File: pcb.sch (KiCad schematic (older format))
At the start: 36 parts, among them J1 230VAC IN, J10 DHT22 2, J11 DHT22 3, J12 LIGHTS, J2 12VDC IN, J3 40HAT, J4 CONN_01X02, J5 CONN_02X02, J6 FAN 1, J7 FAN 2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

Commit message: Rearranged connectors. Added early triac circuit.
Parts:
- added C1: 10u, Capacitor_SMD:CP_Elec_4x5.3, symbol Device:CP
- added Q6: BT136-600, Package_TO_SOT_THT:TO-220-3_Vertical, symbol Triac_Thyristor:BT136-600
- added R4, R5: 400R, Resistor_SMD:R_1206_3216Metric_Pad1.30x1.75mm_HandSolder, symbol Device:R
- added U1: MOC3043M, symbol Relay_SolidState:MOC3043M
- gave numbers to parts that had none: 8
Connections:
- wire segments 136 -> 152
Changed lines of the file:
@@
 	3200 3250 4400 3250
 $Comp
-L Connector_Generic:Conn_01x02 J?
+L Connector_Generic:Conn_01x02 J13
 U 1 1 5FD232CF
 P 12300 4350
-F 0 "J?" H 12380 4342 50  0000 L CNN
+F 0 "J13" H 12380 4342 50  0000 L CNN
 F 1 "Conn_01x02" H 12380 4251 50  0000 L CNN
 F 2 "Connector_PinHeader_2.54mm:PinHeader_1x02_P2.54mm_Vertical" H 12300 4350 50  0001 C CNN
@@
 $EndComp
 $Comp
-L power:GND #PWR?
+L power:GND #PWR0101
 U 1 1 5FD55316
 P 10750 6500
-F 0 "#PWR?" H 10750 6250 50  0001 C CNN
+F 0 "#PWR0101" H 10750 6250 50  0001 C CNN
 F 1 "GND" H 10750 6350 50  0000 C CNN
 F 2 "" H 10750 6500 50  0000 C CNN
@@
 FAN_1_OUT
 $Comp
-L Device:R R?
+L Device:R R1
 U 1 1 5FCE279C
 P 10250 6250
-F 0 "R?" V 10043 6250 50  0000 C CNN
+F 0 "R1" V 10043 6250 50  0000 C CNN
 F 1 "100R" V 10134 6250 50  0000 C CNN
 F 2 "Resistor_SMD:R_1206_3216Metric_Pad1.30x1.75mm_HandSolder" V 10180 6250 50  0001 C CNN
@@
 	11600 4450 12100 4450
 $Comp
-L Connector_Generic:Conn_01x02 J?
+L Connector_Generic:Conn_01x02 J14
 U 1 1 5FF3F3E5
 P 13700 4350
-F 0 "J?" H 13780 4342 50  0000 L CNN
+F 0 "J14" H 13780 4342 50  0000 L CNN
 F 1 "Conn_01x02" H 13780 4251 50  0000 L CNN
 F 2 "Connector_PinHeader_2.54mm:PinHeader_1x02_P2.54mm_Vertical" H 13700 4350 50  0001 C CNN
@@
 	13000 4450 13500 4450
 $Comp
-L Connector_Generic:Conn_01x02 J?
+L Connector_Generic:Conn_01x02 J15
 U 1 1 5FF44AFB
 P 15050 4350
-F 0 "J?" H 15130 4342 50  0000 L CNN
+F 0 "J15" H 15130 4342 50  0000 L CNN
 F 1 "Conn_01x02" H 15130 4251 50  0000 L CNN
 F 2 "Connector_PinHeader_2.54mm:PinHeader_1x02_P2.54mm_Vertical" H 15050 4350 50  0001 C CNN
@@
 	14350 4450 14850 4450
 $Comp
-L plantification:IRLIZ44N Q?
+L plantification:IRLIZ44N Q4
 U 1 1 5FF58F9B
 P 10650 7100
-F 0 "Q?" H 10855 7146 50  0000 L CNN
+F 0 "Q4" H 10855 7146 50  0000 L CNN
 F 1 "IRLU024NPBF" H 10855 7055 50  0000 L CNN
 F 2 "Package_TO_SOT_THT:TO-251-3-1EP_Horizontal_TabDown" H 10900 7025 50  0001 L CIN
@@
 $EndComp
 $Comp
-L power:GND #PWR?
+L power:GND #PWR0102
 U 1 1 5FF58FA1
 P 10750 7350
-F 0 "#PWR?" H 10750 7100 50  0001 C CNN
+F 0 "#PWR0102" H 10750 7100 50  0001 C CNN
 F 1 "GND" H 10750 7200 50  0000 C CNN
 F 2 "" H 10750 7350 50  0000 C CNN
@@
 FAN_2_OUT
 $Comp
-L Device:R R?
+L Device:R R2
 U 1 1 5FF58FAD
 P 10250 7100
-F 0 "R?" V 10043 7100 50  0000 C CNN
+F 0 "R2" V 10043 7100 50  0000 C CNN
 F 1 "100R" V 10134 7100 50  0000 C CNN
 F 2 "Resistor_SMD:R_1206_3216Metric_Pad1.30x1.75mm_HandSolder" V 10180 7100 50  0001 C CNN
@@
 	10100 7100 9500 7100
 $Comp
-L plantification:IRLIZ44N Q?
+L plantification:IRLIZ44N Q5
 U 1 1 5FF5F52E
 P 10650 7950
-F 0 "Q?" H 10855 7996 50  0000 L CNN
+F 0 "Q5" H 10855 7996 50  0000 L CNN
 F 1 "IRLU024NPBF" H 10855 7905 50  0000 L CNN
 F 2 "Package_TO_SOT_THT:TO-251-3-1EP_Horizontal_TabDown" H 10900 7875 50  0001 L CIN
@@
 $EndComp
 $Comp
-L power:GND #PWR?
+L power:GND #PWR0103
 U 1 1 5FF5F534
 P 10750 8200
-F 0 "#PWR?" H 10750 7950 50  0001 C CNN
+F 0 "#PWR0103" H 10750 7950 50  0001 C CNN
 F 1 "GND" H 10750 8050 50  0000 C CNN
 F 2 "" H 10750 8200 50  0000 C CNN
@@
 FAN_3_OUT
 $Comp
-L Device:R R?
+L Device:R R3
 U 1 1 5FF5F540
 P 10250 7950
-F 0 "R?" V 10043 7950 50  0000 C CNN
+F 0 "R3" V 10043 7950 50  0000 C CNN
 F 1 "100R" V 10134 7950 50  0000 C CNN
 F 2 "Resistor_SMD:R_1206_3216Metric_Pad1.30x1.75mm_HandSolder" V 10180 7950 50  0001 C CNN
@@
 Wire Wire Line
 	10100 7950 9500 7950
+$Comp
+L Relay_SolidState:MOC3043M U1
+U 1 1 5FCCF357
+P 13100 6550
+F 0 "U1" H 13100 6875 50  0000 C CNN
+F 1 "MOC3043M" H 13100 6784 50  0000 C CNN
+F 2 "" H 12900 6350 50  0001 L CIN
+F 3 "https://www.onsemi.com/pub/Collateral/MOC3043M-D.pdf" H 13100 6550 50  0001 L CNN
+	1    13100 6550
+	1    0    0    -1
+$EndComp
+$Comp
+L Device:R R4
+U 1 1 5FCD0D80
+P 12600 6450
+F 0 "R4" V 12393 6450 50  0000 C CNN
+F 1 "400R" V 12484 6450 50  0000 C CNN
+F 2 "Resistor_SMD:R_1206_3216Metric_Pad1.30x1.75mm_HandSolder" V 12530 6450 50  0001 C CNN
+F 3 "~" H 12600 6450 50  0001 C CNN
+	1    12600 6450
+	0    1    1    0
+$EndComp
+$Comp
+L Device:CP C1
+U 1 1 5FCD2BE2
+P 12300 6600
+F 0 "C1" H 12418 6646 50  0000 L CNN
+F 1 "10u" H 12418 6555 50  0000 L CNN
+F 2 "Capacitor_SMD:CP_Elec_4x5.3" H 12338 6450 50  0001 C CNN
+F 3 "~" H 12300 6600 50  0001 C CNN
+	1    12300 6600
+	1    0    0    -1
+$EndComp
+$Comp
+L Triac_Thyristor:BT136-600 Q6
+U 1 1 5FCD5F94
+P 14000 6600
+F 0 "Q6" H 14128 6646 50  0000 L CNN
+F 1 "BT136-600" H 14128 6555 50  0000 L CNN
+F 2 "Package_TO_SOT_THT:TO-220-3_Vertical" H 14200 6525 50  0001 L CIN
+F 3 "http://www.micropik.com/PDF/BT136-600.pdf" H 14000 6600 50  0001 L CNN
+	1    14000 6600
+	1    0    0    -1
+$EndComp
+$Comp
+L Device:R R5
+U 1 1 5FCD7A14
+P 13650 6450
+F 0 "R5" V 13443 6450 50  0000 C CNN
+F 1 "400R" V 13534 6450 50  0000 C CNN
+F 2 "Resistor_SMD:R_1206_3216Metric_Pad1.30x1.75mm_HandSolder" V 13580 6450 50  0001 C CNN
+F 3 "~" H 13650 6450 50  0001 C CNN
+	1    13650 6450
+	0    1    1    0
+$EndComp
+Wire Wire Line
+	12750 6450 12800 6450
+Wire Wire Line
+	12450 6450 12300 6450
+Connection ~ 12300 6450
+Wire Wire Line
+	12300 6450 11800 6450
+Wire Wire Line
+	12800 6650 12800 6750
+Wire Wire Line
+	12800 6750 12300 6750
+Wire Wire Line
+	11800 6750 12300 6750
+Connection ~ 12300 6750
+Wire Wire Line
+	13500 6450 13400 6450
+Wire Wire Line
+	13800 6450 14000 6450
+Wire Wire Line
+	13850 6700 13750 6700
+Wire Wire Line
+	13750 6700 13750 6650
+Wire Wire Line
+	13750 6650 13400 6650
+Wire Wire Line
+	14000 6750 14000 6900
+Wire Wire Line
+	14000 6450 14000 6300
+Connection ~ 14000 6450
+Wire Wire Line
+	14000 6300 14500 6300
+Wire Wire Line
+	14000 6900 14500 6900
+Text Label 14500 6900 2    50   ~ 0
+LIGHTS_L
+Text Label 14500 6300 2    50   ~ 0
+230VAC_L
+Text Label 13650 5900 2    50   ~ 0
+LIGHTS_N
+Text Label 12700 5900 0    50   ~ 0
+230VAC_N
+Wire Wire Line
+	12700 5900 13650 5900
 $EndSCHEMATC

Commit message: Set optoisolator and triac footprints
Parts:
- Q6: footprint Package_TO_SOT_THT:TO-220-3_Vertical -> Package_TO_SOT_THT:TO-220-3_Horizontal_TabDown
- U1: footprint (none) -> Package_DIP:DIP-6_W7.62mm
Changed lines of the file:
@@
 F 0 "U1" H 13100 6875 50  0000 C CNN
 F 1 "MOC3043M" H 13100 6784 50  0000 C CNN
-F 2 "" H 12900 6350 50  0001 L CIN
+F 2 "Package_DIP:DIP-6_W7.62mm" H 12900 6350 50  0001 L CIN
 F 3 "https://www.onsemi.com/pub/Collateral/MOC3043M-D.pdf" H 13100 6550 50  0001 L CNN
 	1    13100 6550
@@
 F 0 "Q6" H 14128 6646 50  0000 L CNN
 F 1 "BT136-600" H 14128 6555 50  0000 L CNN
-F 2 "Package_TO_SOT_THT:TO-220-3_Vertical" H 14200 6525 50  0001 L CIN
+F 2 "Package_TO_SOT_THT:TO-220-3_Horizontal_TabDown" H 14200 6525 50  0001 L CIN
 F 3 "http://www.micropik.com/PDF/BT136-600.pdf" H 14000 6600 50  0001 L CNN
 	1    14000 6600

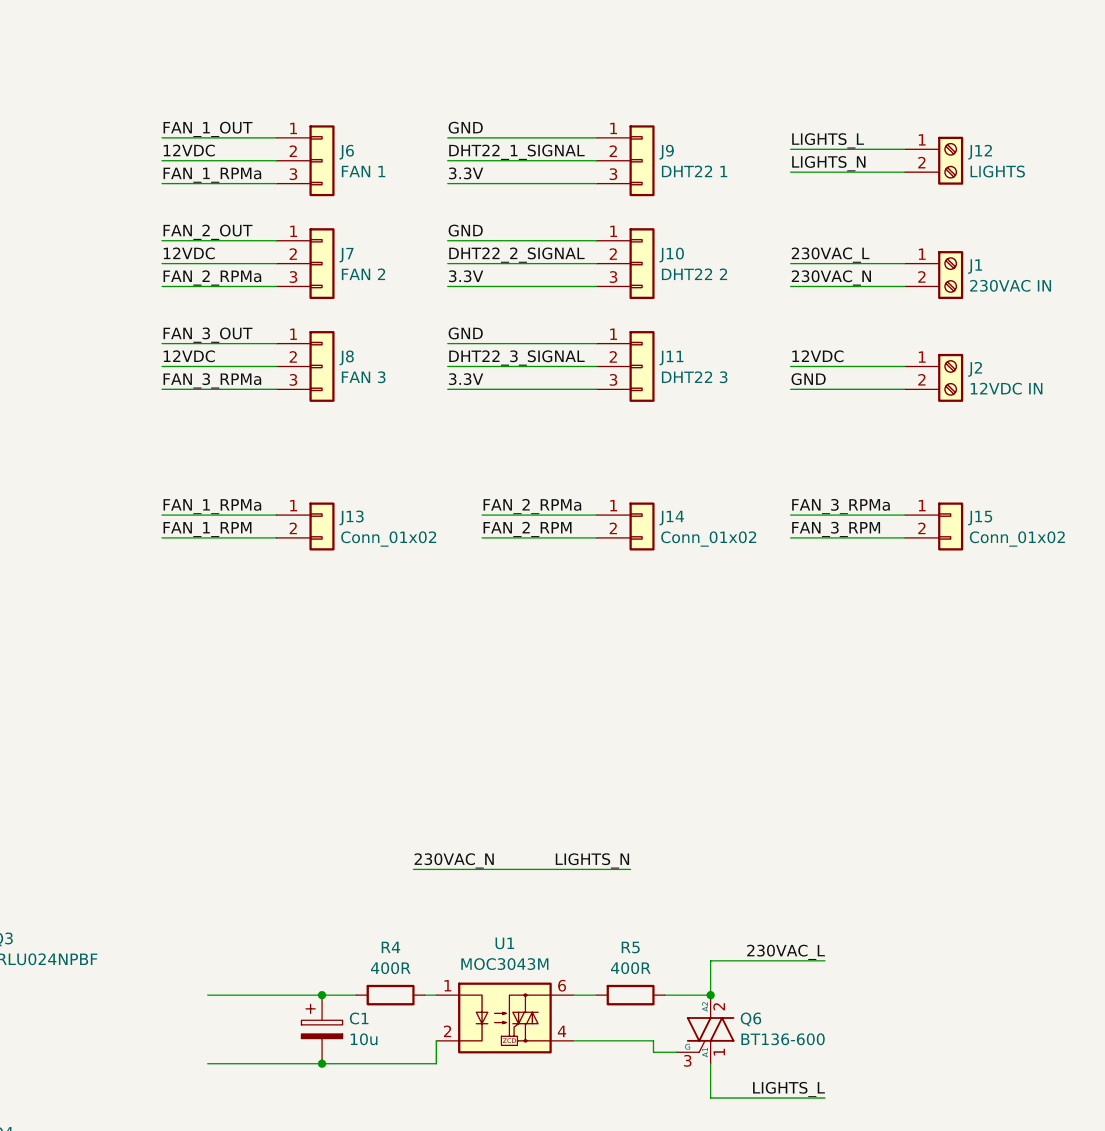
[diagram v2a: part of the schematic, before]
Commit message: Remove fan speed connectors
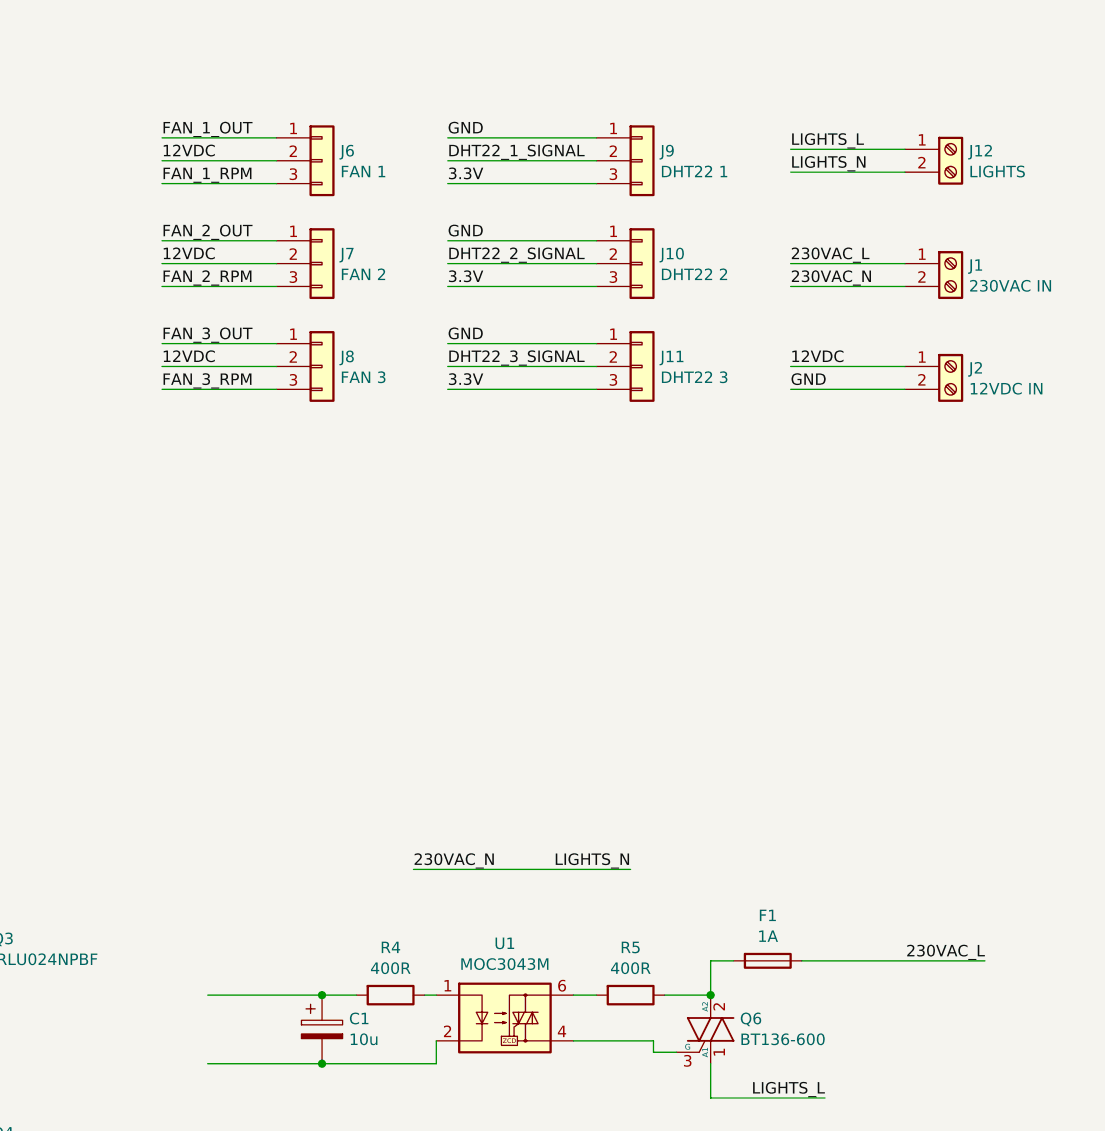
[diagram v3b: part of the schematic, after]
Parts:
- removed J13, J14, J15: Conn_01x02, Connector_PinHeader_2.54mm:PinHeader_1x02_P2.54mm_Vertical, symbol Connector_Generic:Conn_01x02
- added F1: 1A, Fuse:Fuseholder_Cylinder-5x20mm_Schurter_0031_8201_Horizontal_Open, symbol Device:Fuse
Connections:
- net labels removed: FAN_1_RPMa, FAN_2_RPMa, FAN_3_RPMa
- wire segments 152 -> 147
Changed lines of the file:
@@
 12VDC
 Text Label 11600 2900 0    50   ~ 0
-FAN_1_RPMa
+FAN_1_RPM
 Text Label 14350 3250 0    50   ~ 0
 230VAC_L
@@
 FAN_3_OUT
 Text Label 11600 3350 0    50   ~ 0
-FAN_2_RPMa
+FAN_2_RPM
 Text Label 11600 3800 0    50   ~ 0
-FAN_3_RPMa
+FAN_3_RPM
 Text Label 12850 2900 0    50   ~ 0
 3.3V
@@
 	3200 3250 4400 3250
 $Comp
-L Connector_Generic:Conn_01x02 J13
-U 1 1 5FD232CF
-P 12300 4350
-F 0 "J13" H 12380 4342 50  0000 L CNN
-F 1 "Conn_01x02" H 12380 4251 50  0000 L CNN
-F 2 "Connector_PinHeader_2.54mm:PinHeader_1x02_P2.54mm_Vertical" H 12300 4350 50  0001 C CNN
-F 3 "~" H 12300 4350 50  0001 C CNN
-	1    12300 4350
-	1    0    0    -1
-$EndComp
-$Comp
 L power:GND #PWR0101
 U 1 1 5FD55316
@@
 Wire Wire Line
 	14350 3350 14850 3350
-Text Label 11600 4350 0    50   ~ 0
-FAN_1_RPMa
-Text Label 11600 4450 0    50   ~ 0
-FAN_1_RPM
-Wire Wire Line
-	11600 4350 12100 4350
-Wire Wire Line
-	11600 4450 12100 4450
-$Comp
-L Connector_Generic:Conn_01x02 J14
-U 1 1 5FF3F3E5
-P 13700 4350
-F 0 "J14" H 13780 4342 50  0000 L CNN
-F 1 "Conn_01x02" H 13780 4251 50  0000 L CNN
-F 2 "Connector_PinHeader_2.54mm:PinHeader_1x02_P2.54mm_Vertical" H 13700 4350 50  0001 C CNN
-F 3 "~" H 13700 4350 50  0001 C CNN
-	1    13700 4350
-	1    0    0    -1
-$EndComp
-Text Label 13000 4350 0    50   ~ 0
-FAN_2_RPMa
-Text Label 13000 4450 0    50   ~ 0
-FAN_2_RPM
-Wire Wire Line
-	13000 4350 13500 4350
-Wire Wire Line
-	13000 4450 13500 4450
-$Comp
-L Connector_Generic:Conn_01x02 J15
-U 1 1 5FF44AFB
-P 15050 4350
-F 0 "J15" H 15130 4342 50  0000 L CNN
-F 1 "Conn_01x02" H 15130 4251 50  0000 L CNN
-F 2 "Connector_PinHeader_2.54mm:PinHeader_1x02_P2.54mm_Vertical" H 15050 4350 50  0001 C CNN
-F 3 "~" H 15050 4350 50  0001 C CNN
-	1    15050 4350
-	1    0    0    -1
-$EndComp
-Text Label 14350 4350 0    50   ~ 0
-FAN_3_RPMa
-Text Label 14350 4450 0    50   ~ 0
-FAN_3_RPM
-Wire Wire Line
-	14350 4350 14850 4350
-Wire Wire Line
-	14350 4450 14850 4450
 $Comp
 L plantification:IRLIZ44N Q4
@@
 Connection ~ 14000 6450
 Wire Wire Line
-	14000 6300 14500 6300
-Wire Wire Line
 	14000 6900 14500 6900
 Text Label 14500 6900 2    50   ~ 0
 LIGHTS_L
-Text Label 14500 6300 2    50   ~ 0
+Text Label 15200 6300 2    50   ~ 0
 230VAC_L
 Text Label 13650 5900 2    50   ~ 0
@@
 Wire Wire Line
 	12700 5900 13650 5900
+$Comp
+L Device:Fuse F1
+U 1 1 5FCC3312
+P 14250 6300
+F 0 "F1" V 14053 6300 50  0000 C CNN
+F 1 "1A" V 14144 6300 50  0000 C CNN
+F 2 "Fuse:Fuseholder_Cylinder-5x20mm_Schurter_0031_8201_Horizontal_Open" V 14180 6300 50  0001 C CNN
+F 3 "~" H 14250 6300 50  0001 C CNN
+	1    14250 6300
+	0    1    1    0
+$EndComp
+Wire Wire Line
+	14000 6300 14100 6300
+Wire Wire Line
+	14400 6300 15200 6300
 $EndSCHEMATC

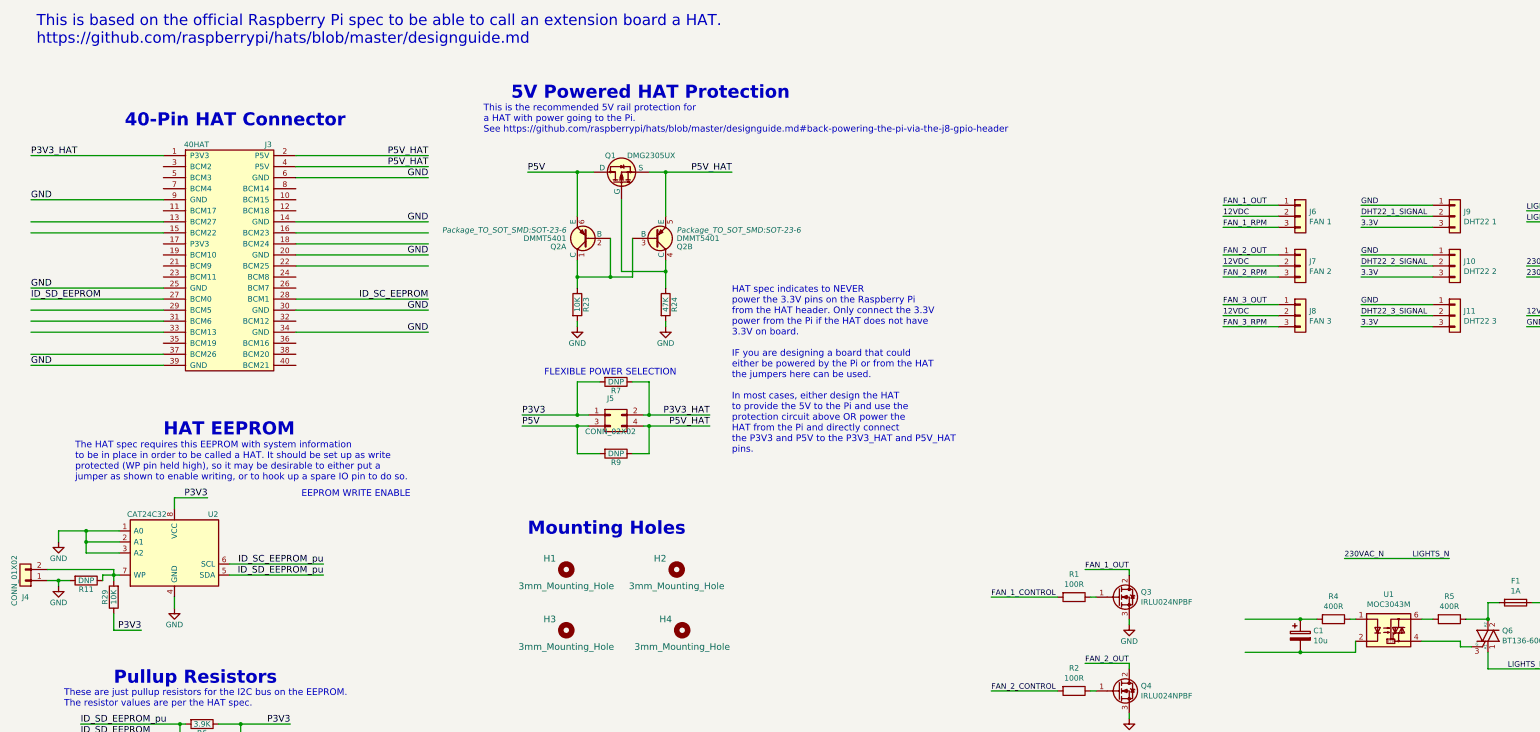
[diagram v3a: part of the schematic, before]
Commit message: Connect devices to the RPi connector
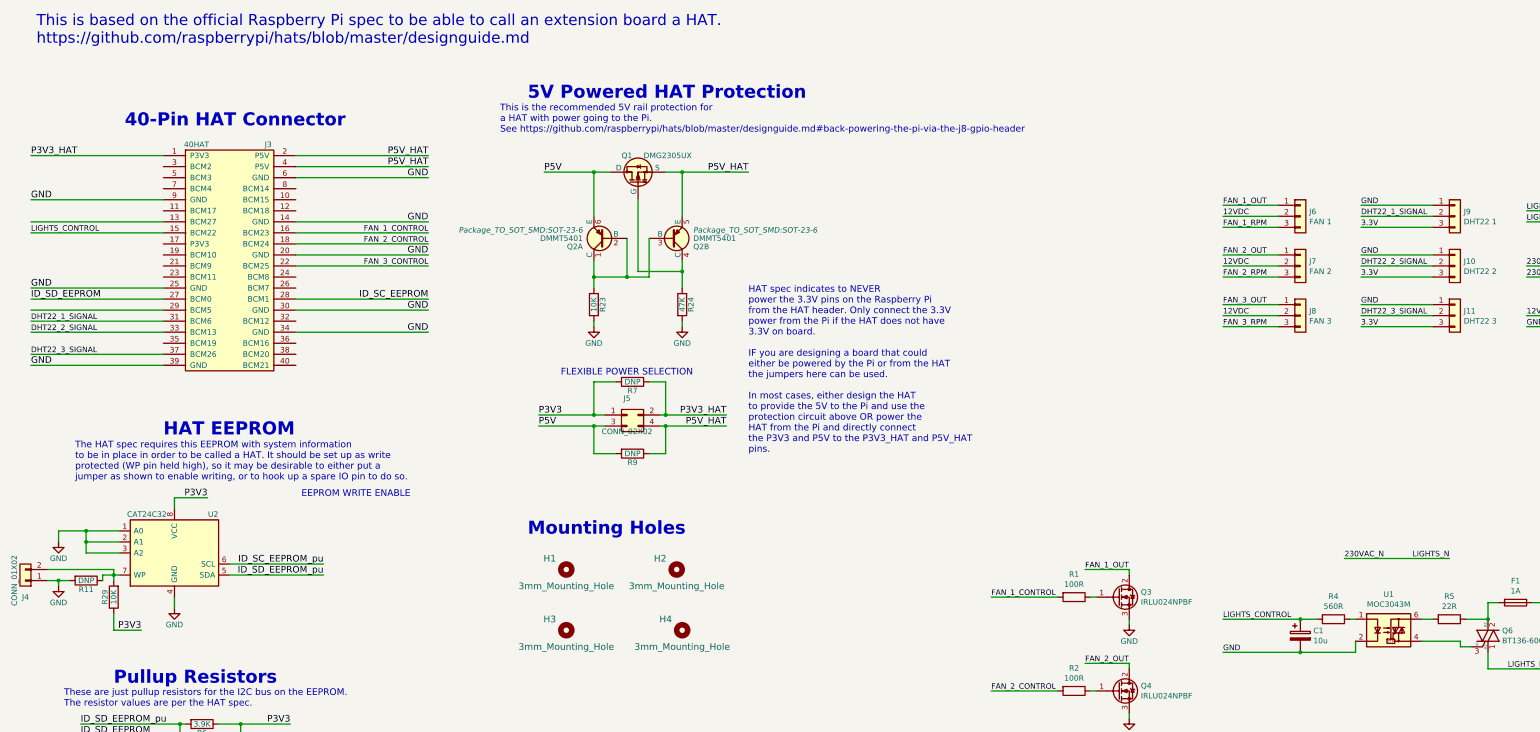
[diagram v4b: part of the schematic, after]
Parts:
- R4: value 400R -> 560R
- R5: value 400R -> 22R
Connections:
- net labels added: LIGHTS_CONTROL
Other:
- moved on the sheet: J5, Q1, Q2A, Q2B, R23, R24, R7, R9
